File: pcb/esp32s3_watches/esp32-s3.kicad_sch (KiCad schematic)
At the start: 11 parts, among them J1 Barrel_Jack_MountingPin, J2 10067847-001RLF, J3 Screw_Terminal_01x02, U1 ESP32-S3-DevKitC

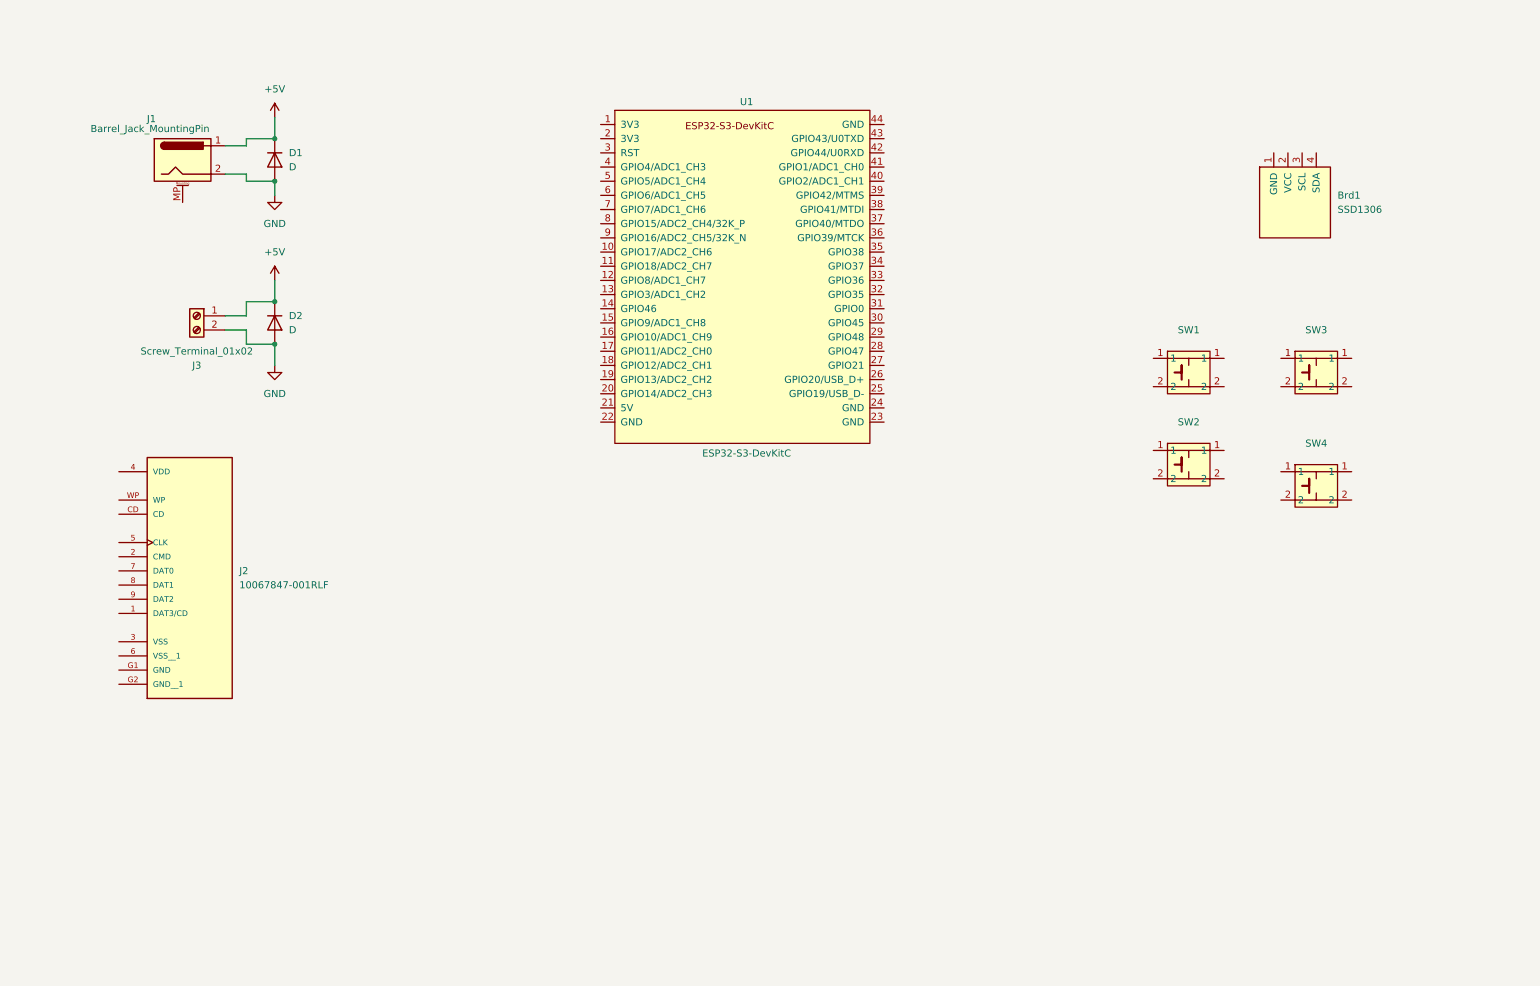
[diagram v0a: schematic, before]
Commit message: Update SD card connection
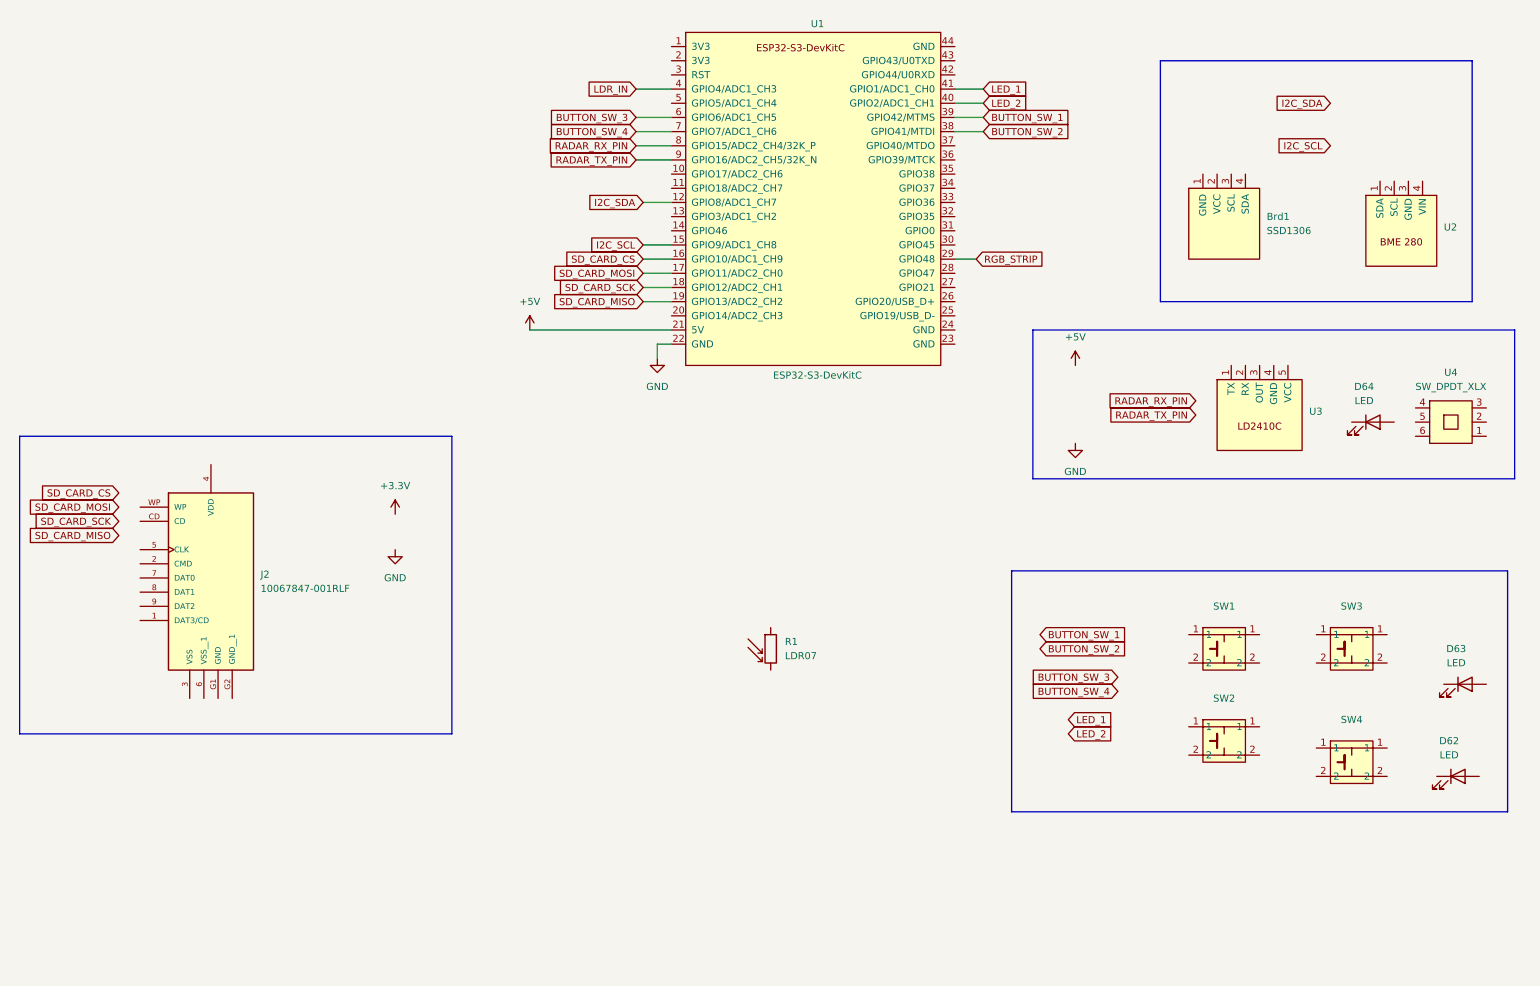
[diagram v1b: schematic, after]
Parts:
- removed D1, D2: D, Diode_SMD:D_PowerDI-123, symbol Device:D
- removed J1: Barrel_Jack_MountingPin, Connector_BarrelJack:BarrelJack_GCT_DCJ200-10-A_Horizontal, symbol Connector:Barrel_Jack_MountingPin
- removed J3: Screw_Terminal_01x02, esp32s3_watches:terminal_block, symbol Connector:Screw_Terminal_01x02
- added D62, D63, D64: LED, LED_THT:LED_D5.0mm, symbol Device:LED
- added R1: LDR07, OptoDevice:R_LDR_5.1x4.3mm_P3.4mm_Vertical, symbol Sensor_Optical:LDR07
- added U2: ~, esp32s3_watches:BME280, symbol esp32s3_watches:BME280
- added U3: ~, esp32s3_watches:LD2410C, symbol esp32s3_watches:LD2410C
- added U4: SW_DPDT_XLX, esp32s3_watches:SW_DPDT_XLX, symbol esp32s3_watches:SW_DPDT_XLX
- J2: footprint 10067847-001RLF:AMPHENOL_10067847-001RLF -> esp32s3_watches:AMPHENOL_10067847-001RLF
- SW1, SW2, SW3, SW4: footprint stm32f401_pcm5102_shiled_lib:SW_PUSH_6mm_H5mm -> esp32s3_watches:SW_PUSH_6mm_H5mm
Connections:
- net +5V: now also U1.21 (5V)
- net GND: now also U1.22 (GND)
- net I2C_SDA: now reaches U1.12 (GPIO8/ADC1_CH7)
- net I2C_SCL: now reaches U1.15 (GPIO9/ADC1_CH8)
- net SD_CARD_CS: now reaches U1.16 (GPIO10/ADC1_CH9)
- net SD_CARD_MOSI: now reaches U1.17 (GPIO11/ADC2_CH0)
- net SD_CARD_SCK: now reaches U1.18 (GPIO12/ADC2_CH1)
- net SD_CARD_MISO: now reaches U1.19 (GPIO13/ADC2_CH2)
- net RGB_STRIP: now reaches U1.29 (GPIO48)
- net BUTTON_SW_2: now reaches U1.38 (GPIO41/MTDI)
- net BUTTON_SW_1: now reaches U1.39 (GPIO42/MTMS)
- net LDR_IN: now reaches U1.4 (GPIO4/ADC1_CH3)
- net LED_2: now reaches U1.40 (GPIO2/ADC1_CH1)
- net LED_1: now reaches U1.41 (GPIO1/ADC1_CH0)
- net BUTTON_SW_3: now reaches U1.6 (GPIO6/ADC1_CH5)
- net BUTTON_SW_4: now reaches U1.7 (GPIO7/ADC1_CH6)
- net RADAR_RX_PIN: now reaches U1.8 (GPIO15/ADC2_CH4/32K_P)
- net RADAR_TX_PIN: now reaches U1.9 (GPIO16/ADC2_CH5/32K_N)
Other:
- moved on the sheet: Brd1, SW1, SW2, SW3, SW4, U1

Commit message: Scheme improvements
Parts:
- added C6: 10uF, symbol Device:C
- added C7, C8: 100nF, symbol Device:C
- added R10, R11, R12, R13, R14, R5, R6, R7, R8: 10kR, symbol Device:R
- added R15, R16, R9: 500R, symbol Device:R
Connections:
- net +3.3V: now also Brd1.2 (VCC), J2.4 (VDD), R1.2, SW1.1, SW2.1, SW3.1, SW4.1, U2.4 (VIN), C6.1, C7.1, R5.1, R6.1, R7.1, R8.1
- net +5V: now also U4.3, U4.4
- net BUTTON_SW_1: now also SW1.2, R11.1
- net BUTTON_SW_2: now also SW2.2, R12.1
- net BUTTON_SW_3: now also SW3.2, R13.1
- net BUTTON_SW_4: now also SW4.2, R14.1
- net GND: now also Brd1.1 (GND), J2.3 (VSS), J2.6 (VSS__1), J2.G1 (GND), J2.G2 (GND__1), U2.3 (GND), U3.4 (GND), U4.1, U4.6, C6.2, C7.2, C8.2, R10.2, R11.2, R12.2, R13.2, R14.2, R15.2, R16.2, R9.2
- net I2C_SCL: now also Brd1.3 (SCL), U2.1 (SDA)
- net I2C_SDA: now also Brd1.4 (SDA), U2.2 (SCL)
- net LDR_IN: now also R1.1, C8.1, R10.1
- net LED_1: now also D62.2 (A)
- net LED_2: now also D63.2 (A)
- net RADAR_RX_PIN: now also U3.1 (TX)
- net RADAR_TX_PIN: now also U3.2 (RX)
- net SD_CARD_CS: now also J2.1 (DAT3/CD), R8.2
- net SD_CARD_MISO: now also J2.7 (DAT0), R7.2
- net SD_CARD_MOSI: now also J2.2 (CMD), R6.2
- net SD_CARD_SCK: now also J2.5 (CLK), R5.2
- net at D62.1 (K): now also R15.1
- net at D63.1 (K): now also R16.1
- net at D64.1 (K): now also R9.1
- net at D64.2 (A): now also U3.3 (OUT)
- net LD2410_VCC: now reaches U4.2
- net LD2410_VCC: now also U3.5 (VCC), U4.5
- no-connect marks 0 -> 29
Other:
- note added: "#define RADAR_RX_PIN 15 // 15 on board is RX connect to TX on RADAR #define RADAR_TX_PIN 16 // 16 on board is TX connect to RX on RADAR"
- note added: "Buttons & LEDs"
- note added: "ESP32 S3 board"
- note added: "LDR"
- note added: "Radar"
- note added: "SD card SPI interface"
- moved on the sheet: Brd1, D62, D63, D64, J2, R1, SW1, SW2, SW3, SW4, U1, U2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

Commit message: BOM file updates. Scheme complete.
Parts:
- added D100, D101, D102, D103, D104: PESD3V3L1BA,115, Diode_SMD:D_SOD-323, symbol Device:D_TVS
- added J101, J102, J103: Conn_01x04_Pin, Connector_PinHeader_1.27mm:PinHeader_1x04_P1.27mm_Vertical, symbol Connector:Conn_01x04_Pin
- C100: renamed from C6; footprint (none) -> Capacitor_SMD:C_0805_2012Metric; Manufacturer (none) -> Samsung Electro-Mechanics; Manufacturer Product Number (none) -> CL21A106KOQNNNE
- C101: renamed from C7; footprint (none) -> Capacitor_SMD:C_0603_1608Metric; Manufacturer (none) -> Samsung Electro-Mechanics; Manufacturer Product Number (none) -> CL10B104KB8NNNC
- C103: renamed from C8; footprint (none) -> Capacitor_SMD:C_0603_1608Metric; Manufacturer (none) -> Samsung Electro-Mechanics; Manufacturer Product Number (none) -> CL10B104KB8NNNC
- J100: renamed from J2; Manufacturer (none) -> Amphenol ICC; Manufacturer Product Number (none) -> 10067847-001RLF
- R100: renamed from R5; footprint (none) -> Resistor_SMD:R_0805_2012Metric; Manufacturer (none) -> UNI-ROYAL(Uniroyal Elec); Manufacturer Product Number (none) -> 0805W8F1002T5E
- R101: renamed from R6; footprint (none) -> Resistor_SMD:R_0805_2012Metric; Manufacturer (none) -> UNI-ROYAL(Uniroyal Elec); Manufacturer Product Number (none) -> 0805W8F1002T5E
- R102: renamed from R7; footprint (none) -> Resistor_SMD:R_0805_2012Metric; Manufacturer (none) -> UNI-ROYAL(Uniroyal Elec); Manufacturer Product Number (none) -> 0805W8F1002T5E
- R103: renamed from R8; footprint (none) -> Resistor_SMD:R_0805_2012Metric; Manufacturer (none) -> UNI-ROYAL(Uniroyal Elec); Manufacturer Product Number (none) -> 0805W8F1002T5E
- R104: renamed from R9; footprint (none) -> Resistor_SMD:R_0805_2012Metric; Manufacturer (none) -> Viking Tech; Manufacturer Product Number (none) -> ARG05FTC5000
- R105: renamed from R1; Manufacturer Part Number GL5528(10-20) -> (none); Manufacturer Product Number (none) -> GL5528(10-20)
- R106: renamed from R10; footprint (none) -> Resistor_SMD:R_0805_2012Metric; Manufacturer (none) -> UNI-ROYAL(Uniroyal Elec); Manufacturer Product Number (none) -> 0805W8F1002T5E
- R107: renamed from R11; footprint (none) -> Resistor_SMD:R_0805_2012Metric; Manufacturer (none) -> UNI-ROYAL(Uniroyal Elec); Manufacturer Product Number (none) -> 0805W8F1002T5E
- R108: renamed from R12; footprint (none) -> Resistor_SMD:R_0805_2012Metric; Manufacturer (none) -> UNI-ROYAL(Uniroyal Elec); Manufacturer Product Number (none) -> 0805W8F1002T5E
- R109: renamed from R13; footprint (none) -> Resistor_SMD:R_0805_2012Metric; Manufacturer (none) -> UNI-ROYAL(Uniroyal Elec); Manufacturer Product Number (none) -> 0805W8F1002T5E
- R110: renamed from R14; footprint (none) -> Resistor_SMD:R_0805_2012Metric; Manufacturer (none) -> UNI-ROYAL(Uniroyal Elec); Manufacturer Product Number (none) -> 0805W8F1002T5E
- R15, R16: footprint (none) -> Resistor_SMD:R_0805_2012Metric; Manufacturer (none) -> Viking Tech; Manufacturer Product Number (none) -> ARG05FTC5000
- renumbered D64 to D105, D62 to D106, D63 to D107, U4 to SW100, SW1 to SW101, SW2 to SW102, SW3 to SW103, SW4 to SW104, U1 to U100, U3 to U101, Brd1 to U102, U2 to U103
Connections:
- net +3.3V: now also D100.1 (A1), J101.4 (Pin_4), J102.4 (Pin_4), J103.4 (Pin_4)
- net +5V: now also J103.3 (Pin_3)
- net GND: now also D100.2 (A2), D101.2 (A2), D102.2 (A2), D103.2 (A2), D104.2 (A2), J101.1 (Pin_1), J102.1 (Pin_1), J103.1 (Pin_1)
- net I2C_SCL: now also J101.3 (Pin_3)
- net I2C_SDA: now also J101.2 (Pin_2)
- net RGB_STRIP: now also J103.2 (Pin_2)
- net SD_CARD_CS: now also D104.1 (A1)
- net SD_CARD_MISO: now also D103.1 (A1)
- net SD_CARD_MOSI: now also D102.1 (A1)
- net SD_CARD_SCK: now also D101.1 (A1)
- net PCF8563_INT: now reaches U100.37 (GPIO40/MTDO)
- net UART_RX: now reaches U100.42 (GPIO44/U0RXD)
- net UART_RX: now also J102.3 (Pin_3)
- net UART_TX: now reaches U100.43 (GPIO43/U0TXD)
- net UART_TX: now also J102.2 (Pin_2)
- no-connect marks 29 -> 27
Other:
- note added: "I2C modules"
- moved on the sheet: R100, R103

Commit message: Split scheme to 2 boards
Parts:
- J101, J102, J103: footprint Connector_PinHeader_1.27mm:PinHeader_1x04_P1.27mm_Vertical -> Connector_PinHeader_2.54mm:PinHeader_1x04_P2.54mm_Vertical
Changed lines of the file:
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@@
 			)
 		)
-		(property "Footprint" "Connector_PinHeader_1.27mm:PinHeader_1x04_P1.27mm_Vertical"
+		(property "Footprint" "Connector_PinHeader_2.54mm:PinHeader_1x04_P2.54mm_Vertical"
 			(at 259.08 154.94 0)
 			(effects
@@
 			)
 		)
-		(property "Footprint" "Connector_PinHeader_1.27mm:PinHeader_1x04_P1.27mm_Vertical"
+		(property "Footprint" "Connector_PinHeader_2.54mm:PinHeader_1x04_P2.54mm_Vertical"
 			(at 176.53 153.67 0)
 			(effects
@@
 			)
 		)
-		(property "Footprint" "Connector_PinHeader_1.27mm:PinHeader_1x04_P1.27mm_Vertical"
+		(property "Footprint" "Connector_PinHeader_2.54mm:PinHeader_1x04_P2.54mm_Vertical"
 			(at 215.9 153.67 0)
 			(effects
